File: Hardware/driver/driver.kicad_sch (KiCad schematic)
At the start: 8 parts, among them U101 PCA9557PW, U102 DS2482-100

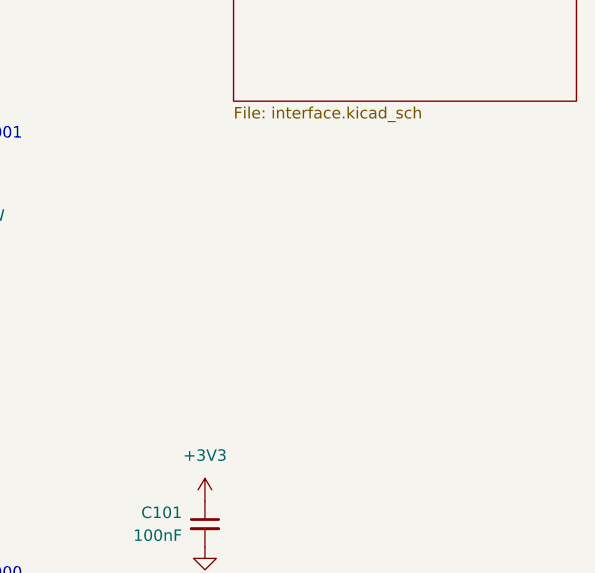
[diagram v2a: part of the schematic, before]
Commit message: Added mains supply input
- The driver board contains a switching mains supply that will give us
  the 12V the system needs, as if by magic

- More work on layout, basically placed the output MOSFETs and stuff
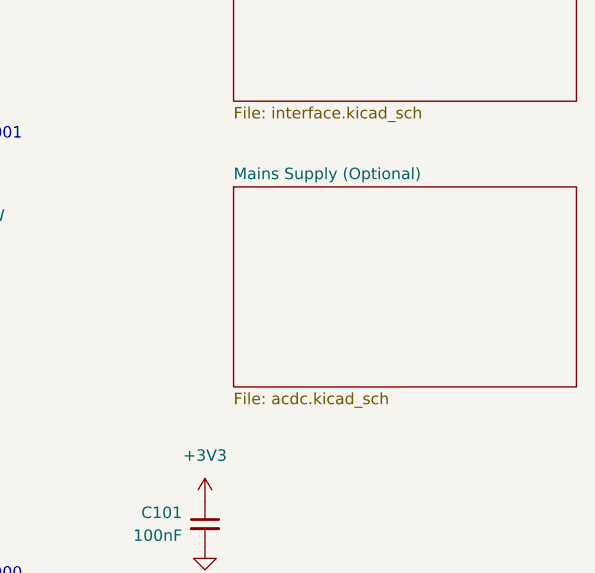
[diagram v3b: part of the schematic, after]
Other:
- added sheet Mains Supply (Optional) (acdc.kicad_sch)
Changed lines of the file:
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@@
+    )
+  )
+  (sheet (at 241.3 85.725) (size 38.1 22.225) (fields_autoplaced)
+    (stroke (width 0.1524) (type solid) (color 0 0 0 0))
+    (fill (color 0 0 0 0.0000))
+    (property "Sheet name" "Mains Supply (Optional)" (id 0) (at 241.3 85.0134 0)
+      (effects (font (size 1.27 1.27)) (justify left bottom))
+    )
+    (property "Sheet file" "acdc.kicad_sch" (id 1) (at 241.3 108.5346 0)
+      (effects (font (size 1.27 1.27)) (justify left top))
     )
   )
@@
     (path "/b8df6840-ecc7-4e2f-ad45-8c79faac2b74" (page "2"))
     (path "/602636dc-d049-47b5-aa22-9e4cd7a5ce25" (page "3"))
+    (path "/e84c78e9-1bd1-4873-b52a-cb877e8caf7e" (page "4"))
   )
   (symbol_instances
+    (path "/e84c78e9-1bd1-4873-b52a-cb877e8caf7e/10929503-cb1d-42a8-9682-d161dba0b501"
+      (reference "#FLG0401") (unit 1) (value "PWR_FLAG") (footprint "")
+    )
     (path "/73e2f12b-9dde-46d3-aecb-771bd98a1295"
       (reference "#PWR0101") (unit 1) (value "+3V3") (footprint "")
@@
       (reference "#PWR0111") (unit 1) (value "GND") (footprint "")
     )
+    (path "/602636dc-d049-47b5-aa22-9e4cd7a5ce25/84073d79-231a-4b9e-b7af-849a8f0779f6"
+      (reference "#PWR0112") (unit 1) (value "GNDPWR") (footprint "")
+    )
+    (path "/602636dc-d049-47b5-aa22-9e4cd7a5ce25/e3dc9e31-87d7-46cc-b364-c30f3dfc81c5"
+      (reference "#PWR0113") (unit 1) (value "VBUS") (footprint "")
+    )
+    (path "/602636dc-d049-47b5-aa22-9e4cd7a5ce25/29af4809-3c28-4637-8aac-999fc4dead91"
+      (reference "#PWR0114") (unit 1) (value "VBUS") (footprint "")
+    )
+    (path "/602636dc-d049-47b5-aa22-9e4cd7a5ce25/3ffffe30-3afd-402e-bd50-928af8a99be2"
+      (reference "#PWR0115") (unit 1) (value "GNDPWR") (footprint "")
+    )
+    (path "/e84c78e9-1bd1-4873-b52a-cb877e8caf7e/44ceed4d-02f1-4589-87bb-12242eec59cf"
+      (reference "#PWR0116") (unit 1) (value "GNDA") (footprint "")
+    )
+    (path "/e84c78e9-1bd1-4873-b52a-cb877e8caf7e/0c0155d8-438f-482e-800f-d1b9570b6b6a"
+      (reference "#PWR0117") (unit 1) (value "GNDA") (footprint "")
+    )
     (path "/b8df6840-ecc7-4e2f-ad45-8c79faac2b74/5cc426dc-ea3e-4d4f-8540-3d6f6e72fffe"
       (reference "#PWR0201") (unit 1) (value "+3V3") (footprint "")
@@
       (reference "#PWR0333") (unit 1) (value "GND") (footprint "")
     )
+    (path "/e84c78e9-1bd1-4873-b52a-cb877e8caf7e/c3bbf127-26eb-40b4-8040-08a58b96616d"
+      (reference "#PWR0401") (unit 1) (value "+12VA") (footprint "")
+    )
+    (path "/e84c78e9-1bd1-4873-b52a-cb877e8caf7e/36945865-03f5-43aa-bb5b-dade85eda7f6"
+      (reference "#PWR0402") (unit 1) (value "+12VA") (footprint "")
+    )
+    (path "/e84c78e9-1bd1-4873-b52a-cb877e8caf7e/4adb21e8-f876-41d7-9dd8-8ca6a1e4f3be"
+      (reference "#PWR0403") (unit 1) (value "+12VA") (footprint "")
+    )
+    (path "/e84c78e9-1bd1-4873-b52a-cb877e8caf7e/860de0d9-c4e6-447c-b450-634d970a47f3"
+      (reference "#PWR0404") (unit 1) (value "GNDA") (footprint "")
+    )
     (path "/52f97038-29ea-412d-a376-537b28ccdcce"
       (reference "C101") (unit 1) (value "100nF") (footprint "Capacitor_SMD:C_0805_2012Metric_Pad1.18x1.45mm_HandSolder")
@@
     )
     (path "/602636dc-d049-47b5-aa22-9e4cd7a5ce25/060e6764-6abf-4c97-a245-94db8f43711d"
-      (reference "C304") (unit 1) (value "33pF") (footprint "")
+      (reference "C304") (unit 1) (value "33pF") (footprint "Capacitor_SMD:C_0805_2012Metric_Pad1.18x1.45mm_HandSolder")
     )
     (path "/602636dc-d049-47b5-aa22-9e4cd7a5ce25/2806be2d-f2a8-42ed-bc80-3d0d995308c1"
@@
       (reference "C309") (unit 1) (value "100nF") (footprint "Capacitor_SMD:C_0805_2012Metric_Pad1.18x1.45mm_HandSolder")
     )
+    (path "/e84c78e9-1bd1-4873-b52a-cb877e8caf7e/71032e47-60f9-4ba5-a483-3e88722fc68e"
+      (reference "C401") (unit 1) (value "1µF") (footprint "Capacitor_SMD:C_0805_2012Metric_Pad1.18x1.45mm_HandSolder")
+    )
+    (path "/e84c78e9-1bd1-4873-b52a-cb877e8caf7e/57bb06df-608c-451b-899a-27d4cf2abef2"
+      (reference "C402") (unit 1) (value "330µF") (footprint "Capacitor_THT:CP_Radial_D8.0mm_P3.50mm")
+    )
+    (path "/e84c78e9-1bd1-4873-b52a-cb877e8caf7e/339c7096-5cf3-4080-9c52-509d29999590"
+      (reference "C403") (unit 1) (value "330µF") (footprint "Capacitor_THT:CP_Radial_D8.0mm_P3.50mm")
+    )
     (path "/b8df6840-ecc7-4e2f-ad45-8c79faac2b74/a1ec3593-f943-4c15-980d-b287c6ade4a4"
-      (reference "D201") (unit 1) (value "Green") (footprint "")
+      (reference "D201") (unit 1) (value "Green") (footprint "LED_SMD:LED_0805_2012Metric_Pad1.15x1.40mm_HandSolder")
     )
     (path "/b8df6840-ecc7-4e2f-ad45-8c79faac2b74/711526a0-0a07-4709-b556-57ae70bd39f2"
-      (reference "D202") (unit 1) (value "Red") (footprint "")
+      (reference "D202") (unit 1) (value "Red") (footprint "LED_SMD:LED_0805_2012Metric_Pad1.15x1.40mm_HandSolder")
+    )
+    (path "/e84c78e9-1bd1-4873-b52a-cb877e8caf7e/03288cb1-6505-446e-b653-9038eaafb14d"
+      (reference "D401") (unit 1) (value "SM6T22A") (footprint "Diode_SMD:D_SMB")
+    )
+    (path "/e84c78e9-1bd1-4873-b52a-cb877e8caf7e/c4cc3695-7194-44cb-add9-d5ccce427833"
+      (reference "D402") (unit 1) (value "Green") (footprint "LED_SMD:LED_0805_2012Metric_Pad1.15x1.40mm_HandSolder")
     )
     (path "/602636dc-d049-47b5-aa22-9e4cd7a5ce25/466ecc93-6956-4bc2-babb-04638a851c6a"
@@
     )
     (path "/b8df6840-ecc7-4e2f-ad45-8c79faac2b74/f83f0a9a-85dc-4ae3-8b32-8863f8282cd1"
-      (reference "J201") (unit 1) (value "Conn_02x10_Odd_Even") (footprint "Connector_PinHeader_1.27mm:PinHeader_2x10_P1.27mm_Vertical_SMD")
+      (reference "J201") (unit 1) (value "Conn_02x10_Odd_Even") (footprint "Connector_IDC:IDC-Header_2x10_P2.54mm_Vertical")
     )
     (path "/602636dc-d049-47b5-aa22-9e4cd7a5ce25/63fdf478-0c5f-4fcd-a9b4-dd10d581d81b"
       (reference "J301") (unit 1) (value "TBP01R2W-508-02BE") (footprint "programmable-load:CUI_TBP01R2W-508-02BE")
     )
+    (path "/e84c78e9-1bd1-4873-b52a-cb877e8caf7e/ac127401-9557-44c6-bdd3-d4dc61661b7d"
+      (reference "J401") (unit 1) (value "TBP02R2W-381-03BE") (footprint "programmable-load:CUI_TBP02R2W-381-03BE")
+    )
+    (path "/e84c78e9-1bd1-4873-b52a-cb877e8caf7e/2389267e-b39e-4057-980a-d385ac0cb8f8"
+      (reference "J402") (unit 1) (value "Conn_01x02_Male") (footprint "Connector_JST:JST_VH_B2P-VH-B_1x02_P3.96mm_Vertical")
+    )
     (path "/b8df6840-ecc7-4e2f-ad45-8c79faac2b74/d4ac8343-5523-4410-b762-44a3c8203733"
       (reference "JP201") (unit 1) (value "Cfg WP") (footprint "")
@@
       (reference "L202") (unit 1) (value "10µH") (footprint "Inductor_SMD:L_1210_3225Metric")
     )
+    (path "/e84c78e9-1bd1-4873-b52a-cb877e8caf7e/87712d96-fe96-4de5-8021-df0987524449"
+      (reference "L401") (unit 1) (value "Choke") (footprint "programmable-load:TDK-ACM1513-0-0-MFG")
+    )
     (path "/b8df6840-ecc7-4e2f-ad45-8c79faac2b74/e1b46ab0-bf3d-472b-9d15-15471e9bef81"
       (reference "M201") (unit 1) (value "Fan_4pin") (footprint "Connector_Molex:Molex_KK-254_AE-6410-04A_1x04_P2.54mm_Vertical")
@@
       (reference "PS201") (unit 1) (value "MEE1S0503SC") (footprint "Converter_DCDC:Converter_DCDC_Murata_MEE1SxxxxSC_THT")
     )
+    (path "/e84c78e9-1bd1-4873-b52a-cb877e8caf7e/05e84446-74e5-4636-a087-5fe6709b524a"
+      (reference "PS401") (unit 1) (value "PSK-S20C-12") (footprint "programmable-load:CONV_PSK-S20C-12")
+    )
     (path "/b8df6840-ecc7-4e2f-ad45-8c79faac2b74/4ec592a9-1618-41f4-a122-c8d720ef8bfb"
       (reference "Q201") (unit 1) (value "MMBT3904") (footprint "Package_TO_SOT_SMD:SOT-23")
@@
       (reference "Q202") (unit 1) (value "PN2222A") (footprint "Package_TO_SOT_THT:TO-92_Inline")
     )
+    (path "/602636dc-d049-47b5-aa22-9e4cd7a5ce25/2cdc59dd-1a7b-4afd-896b-6dd1d45af6c5"
+      (reference "Q301") (unit 1) (value "IXTH80N075L2") (footprint "Package_TO_SOT_THT:TO-247-3_Vertical")
+    )
+    (path "/602636dc-d049-47b5-aa22-9e4cd7a5ce25/68f973a4-135d-4d45-9f49-6504b090328f"
+      (reference "Q302") (unit 1) (value "IXTH80N075L2") (footprint "Package_TO_SOT_THT:TO-247-3_Vertical")
+    )
     (path "/b8df6840-ecc7-4e2f-ad45-8c79faac2b74/1cea6cbb-fc17-4bfd-8441-0eba2acc24a7"
       (reference "R201") (unit 1) (value "2k2") (footprint "Resistor_SMD:R_0805_2012Metric_Pad1.20x1.40mm_HandSolder")
@@
     )
     (path "/602636dc-d049-47b5-aa22-9e4cd7a5ce25/bfc0d8f2-552a-4c02-8d6d-72824aeb58f8"
-      (reference "R302") (unit 1) (value "3k16 .1%") (footprint "Resistor_SMD:R_1206_3216Metric_Pad1.30x1.75mm_HandSolder")
+      (reference "R302") (unit 1) (value "4k53 .1%") (footprint "Resistor_SMD:R_1206_3216Metric_Pad1.30x1.75mm_HandSolder")
+    )
+    (path "/602636dc-d049-47b5-aa22-9e4cd7a5ce25/3d1ab081-ab9e-426b-b1e4-f33218debc94"
+      (reference "R303") (unit 1) (value ".1R") (footprint "Package_TO_SOT_THT:TO-247-2_Vertical")
+    )
+    (path "/602636dc-d049-47b5-aa22-9e4cd7a5ce25/007c0a4c-600e-4e39-898c-fdba374a0c3c"
+      (reference "R304") (unit 1) (value ".1R") (footprint "Package_TO_SOT_THT:TO-247-2_Vertical")
+    )
+    (path "/e84c78e9-1bd1-4873-b52a-cb877e8caf7e/70371ae3-d108-4218-8fc3-6fbe5974fdf4"
+      (reference "R401") (unit 1) (value "4k7") (footprint "Resistor_SMD:R_0805_2012Metric_Pad1.20x1.40mm_HandSolder")
+    )
+    (path "/e84c78e9-1bd1-4873-b52a-cb877e8caf7e/43b11400-816a-4647-b961-3e48b358a013"
+      (reference "RV401") (unit 1) (value "270V") (footprint "Varistor:RV_Disc_D7mm_W4.2mm_P5mm")
     )
     (path "/bd76c248-ba6d-454c-a10f-dbba9b84a653"
@@
     )
     (path "/602636dc-d049-47b5-aa22-9e4cd7a5ce25/a914fe05-f89d-45a1-b276-519d81788838"
-      (reference "U301") (unit 1) (value "MCP3426-xMS") (footprint "")
+      (reference "U301") (unit 1) (value "MCP3426-xMS") (footprint "Package_SO:MSOP-8_3x3mm_P0.65mm")
     )
     (path "/602636dc-d049-47b5-aa22-9e4cd7a5ce25/f8d6c1f5-8cd4-4b9f-937c-2f1e1a9d12d7"

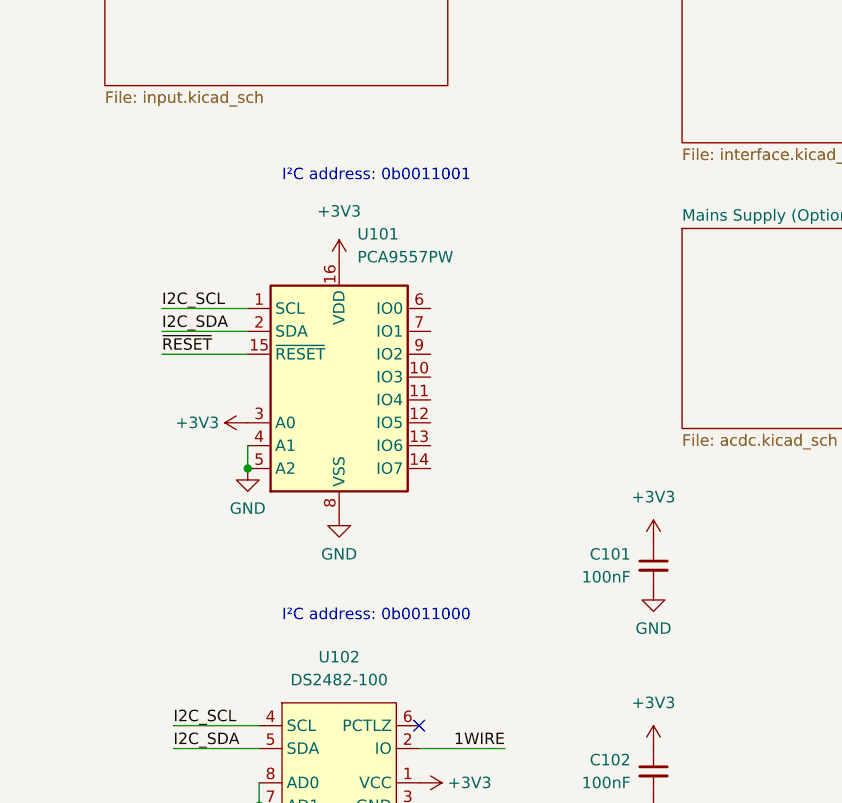
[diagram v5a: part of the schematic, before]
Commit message: Mostly finished routing driver board
- All traces are routed (including some big ass planes for the power
  section; these should be good to roughly 40A) and the board is
  probably good to go.

  It could use with some decorating in the bonus area though :)
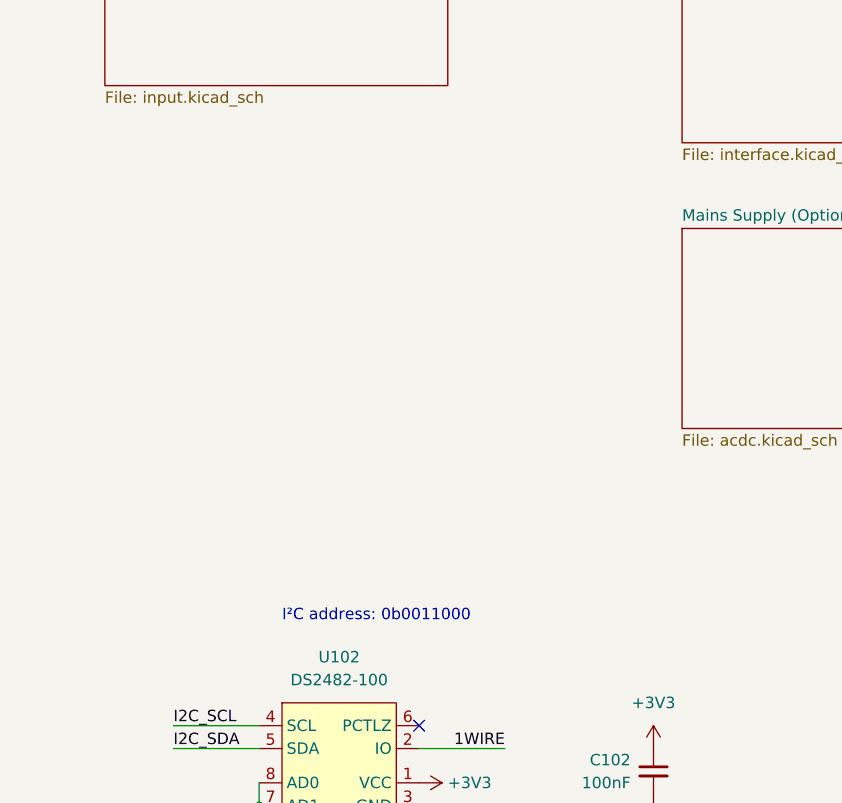
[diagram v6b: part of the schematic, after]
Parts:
- removed C101: 100nF, Capacitor_SMD:C_0805_2012Metric_Pad1.18x1.45mm_HandSolder, symbol Device:C_Small
- removed U101: PCA9557PW, Package_SO:TSSOP-16_4.4x5mm_P0.65mm, symbol Interface_Expansion:PCA9557PW
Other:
- note removed: "I²C address: 0b0011001"
